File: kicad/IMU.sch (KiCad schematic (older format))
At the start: 3 parts, among them U6 ICM-20602

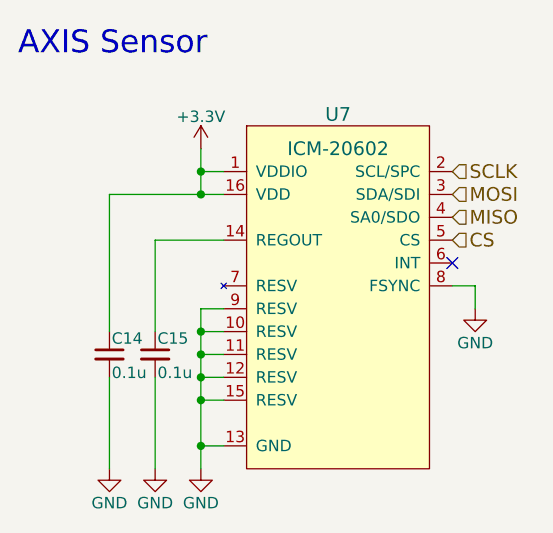
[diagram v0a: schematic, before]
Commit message: 回路にMA702を追加
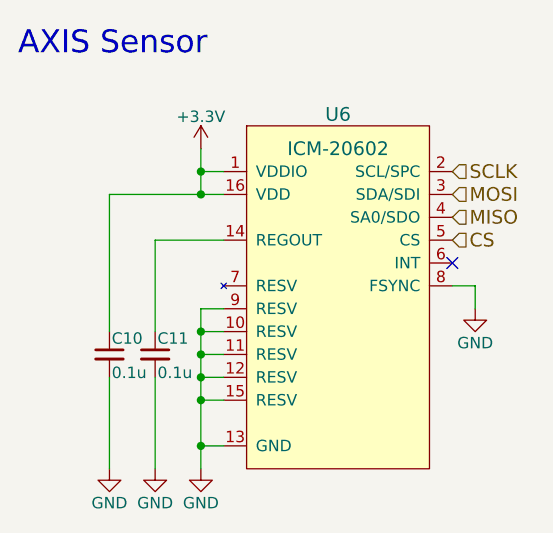
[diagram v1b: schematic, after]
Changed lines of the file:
@@
 AR Path="/57CC33F6/592C611A" Ref="U6"  Part="1"
 AR Path="/5A18D4D6/592C611A" Ref="U7"  Part="1"
-F 0 "U7" H 5600 4150 60  0000 C CNN
+F 0 "U6" H 5600 4150 60  0000 C CNN
 F 1 "ICM-20602" H 5600 4000 60  0000 C CNN
 F 2 "mouse:ICM-20602" H 5600 4000 60  0001 C CNN
@@
 AR Path="/57CC33F6/592C613A" Ref="C11"  Part="1"
 AR Path="/5A18D4D6/592C613A" Ref="C15"  Part="1"
-F 0 "C15" H 4810 3770 50  0000 L CNN
+F 0 "C11" H 4810 3770 50  0000 L CNN
 F 1 "0.1u" H 4810 3620 50  0000 L CNN
 F 2 "Capacitors_SMD:C_0201_NoSilk" H 4800 3700 50  0001 C CNN
@@
 AR Path="/57CC33F6/592C6186" Ref="C10"  Part="1"
 AR Path="/5A18D4D6/592C6186" Ref="C14"  Part="1"
-F 0 "C14" H 4610 3770 50  0000 L CNN
+F 0 "C10" H 4610 3770 50  0000 L CNN
 F 1 "0.1u" H 4610 3620 50  0000 L CNN
 F 2 "Capacitors_SMD:C_0201_NoSilk" H 4600 3700 50  0001 C CNN
@@
 AR Path="/57CC33F6/592C63E1" Ref="#PWR050"  Part="1"
 AR Path="/5A18D4D6/592C63E1" Ref="#PWR061"  Part="1"
-F 0 "#PWR061" H 5000 3950 50  0001 C CNN
+F 0 "#PWR050" H 5000 3950 50  0001 C CNN
 F 1 "GND" H 5000 4050 50  0000 C CNN
 F 2 "" H 5000 4200 50  0000 C CNN
@@
 AR Path="/57CC33F6/592C640D" Ref="#PWR048"  Part="1"
 AR Path="/5A18D4D6/592C640D" Ref="#PWR059"  Part="1"
-F 0 "#PWR059" H 4800 3950 50  0001 C CNN
+F 0 "#PWR048" H 4800 3950 50  0001 C CNN
 F 1 "GND" H 4800 4050 50  0000 C CNN
 F 2 "" H 4800 4200 50  0000 C CNN
@@
 AR Path="/57CC33F6/592C6444" Ref="#PWR047"  Part="1"
 AR Path="/5A18D4D6/592C6444" Ref="#PWR058"  Part="1"
-F 0 "#PWR058" H 4600 3950 50  0001 C CNN
+F 0 "#PWR047" H 4600 3950 50  0001 C CNN
 F 1 "GND" H 4600 4050 50  0000 C CNN
 F 2 "" H 4600 4200 50  0000 C CNN
@@
 AR Path="/57CC33F6/592C64FB" Ref="#PWR049"  Part="1"
 AR Path="/5A18D4D6/592C64FB" Ref="#PWR060"  Part="1"
-F 0 "#PWR060" H 5000 2650 50  0001 C CNN
+F 0 "#PWR049" H 5000 2650 50  0001 C CNN
 F 1 "+3.3V" H 5000 2940 50  0000 C CNN
 F 2 "" H 5000 2800 50  0000 C CNN
@@
 AR Path="/57CC33F6/592C6B85" Ref="#PWR051"  Part="1"
 AR Path="/5A18D4D6/592C6B85" Ref="#PWR062"  Part="1"
-F 0 "#PWR062" H 6200 3250 50  0001 C CNN
+F 0 "#PWR051" H 6200 3250 50  0001 C CNN
 F 1 "GND" H 6200 3350 50  0000 C CNN
 F 2 "" H 6200 3500 50  0000 C CNN

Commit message: コンデンサを追加
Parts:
- renumbered C10 to C11, C11 to C12
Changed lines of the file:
@@
 AR Path="/57CC33F6/592C611A" Ref="U6"  Part="1"
 AR Path="/5A18D4D6/592C611A" Ref="U7"  Part="1"
-F 0 "U6" H 5600 4150 60  0000 C CNN
+F 0 "U7" H 5600 4150 60  0000 C CNN
 F 1 "ICM-20602" H 5600 4000 60  0000 C CNN
 F 2 "mouse:ICM-20602" H 5600 4000 60  0001 C CNN
@@
 $EndComp
 $Comp
-L Device:C_Small C11
+L Device:C_Small C12
 U 1 1 592C613A
 P 4800 3700
-AR Path="/57CC33F6/592C613A" Ref="C11"  Part="1"
-AR Path="/5A18D4D6/592C613A" Ref="C15"  Part="1"
-F 0 "C11" H 4810 3770 50  0000 L CNN
+AR Path="/57CC33F6/592C613A" Ref="C12"  Part="1"
+AR Path="/5A18D4D6/592C613A" Ref="C16"  Part="1"
+F 0 "C16" H 4810 3770 50  0000 L CNN
 F 1 "0.1u" H 4810 3620 50  0000 L CNN
 F 2 "Capacitors_SMD:C_0201_NoSilk" H 4800 3700 50  0001 C CNN
@@
 $EndComp
 $Comp
-L Device:C_Small C10
+L Device:C_Small C11
 U 1 1 592C6186
 P 4600 3700
-AR Path="/57CC33F6/592C6186" Ref="C10"  Part="1"
-AR Path="/5A18D4D6/592C6186" Ref="C14"  Part="1"
-F 0 "C10" H 4610 3770 50  0000 L CNN
+AR Path="/57CC33F6/592C6186" Ref="C11"  Part="1"
+AR Path="/5A18D4D6/592C6186" Ref="C15"  Part="1"
+F 0 "C15" H 4610 3770 50  0000 L CNN
 F 1 "0.1u" H 4610 3620 50  0000 L CNN
 F 2 "Capacitors_SMD:C_0201_NoSilk" H 4600 3700 50  0001 C CNN
@@
 $EndComp
 $Comp
-L power:GND #PWR050
+L power:GND #PWR052
 U 1 1 592C63E1
 P 5000 4200
-AR Path="/57CC33F6/592C63E1" Ref="#PWR050"  Part="1"
-AR Path="/5A18D4D6/592C63E1" Ref="#PWR061"  Part="1"
-F 0 "#PWR061" H 5000 3950 50  0001 C CNN
+AR Path="/57CC33F6/592C63E1" Ref="#PWR052"  Part="1"
+AR Path="/5A18D4D6/592C63E1" Ref="#PWR063"  Part="1"
+F 0 "#PWR063" H 5000 3950 50  0001 C CNN
 F 1 "GND" H 5000 4050 50  0000 C CNN
 F 2 "" H 5000 4200 50  0000 C CNN
@@
 $EndComp
 $Comp
-L power:GND #PWR048
+L power:GND #PWR050
 U 1 1 592C640D
 P 4800 4200
-AR Path="/57CC33F6/592C640D" Ref="#PWR048"  Part="1"
-AR Path="/5A18D4D6/592C640D" Ref="#PWR059"  Part="1"
-F 0 "#PWR059" H 4800 3950 50  0001 C CNN
+AR Path="/57CC33F6/592C640D" Ref="#PWR050"  Part="1"
+AR Path="/5A18D4D6/592C640D" Ref="#PWR061"  Part="1"
+F 0 "#PWR061" H 4800 3950 50  0001 C CNN
 F 1 "GND" H 4800 4050 50  0000 C CNN
 F 2 "" H 4800 4200 50  0000 C CNN
@@
 $EndComp
 $Comp
-L power:GND #PWR047
+L power:GND #PWR049
 U 1 1 592C6444
 P 4600 4200
-AR Path="/57CC33F6/592C6444" Ref="#PWR047"  Part="1"
-AR Path="/5A18D4D6/592C6444" Ref="#PWR058"  Part="1"
-F 0 "#PWR058" H 4600 3950 50  0001 C CNN
+AR Path="/57CC33F6/592C6444" Ref="#PWR049"  Part="1"
+AR Path="/5A18D4D6/592C6444" Ref="#PWR060"  Part="1"
+F 0 "#PWR060" H 4600 3950 50  0001 C CNN
 F 1 "GND" H 4600 4050 50  0000 C CNN
 F 2 "" H 4600 4200 50  0000 C CNN
@@
 $EndComp
 $Comp
-L power:+3.3V #PWR049
+L power:+3.3V #PWR051
 U 1 1 592C64FB
 P 5000 2800
-AR Path="/57CC33F6/592C64FB" Ref="#PWR049"  Part="1"
-AR Path="/5A18D4D6/592C64FB" Ref="#PWR060"  Part="1"
-F 0 "#PWR060" H 5000 2650 50  0001 C CNN
+AR Path="/57CC33F6/592C64FB" Ref="#PWR051"  Part="1"
+AR Path="/5A18D4D6/592C64FB" Ref="#PWR062"  Part="1"
+F 0 "#PWR062" H 5000 2650 50  0001 C CNN
 F 1 "+3.3V" H 5000 2940 50  0000 C CNN
 F 2 "" H 5000 2800 50  0000 C CNN
@@
 NoConn ~ 6100 3300
 $Comp
-L power:GND #PWR051
+L power:GND #PWR053
 U 1 1 592C6B85
 P 6200 3500
-AR Path="/57CC33F6/592C6B85" Ref="#PWR051"  Part="1"
-AR Path="/5A18D4D6/592C6B85" Ref="#PWR062"  Part="1"
-F 0 "#PWR062" H 6200 3250 50  0001 C CNN
+AR Path="/57CC33F6/592C6B85" Ref="#PWR053"  Part="1"
+AR Path="/5A18D4D6/592C6B85" Ref="#PWR064"  Part="1"
+F 0 "#PWR064" H 6200 3250 50  0001 C CNN
 F 1 "GND" H 6200 3350 50  0000 C CNN
 F 2 "" H 6200 3500 50  0000 C CNN

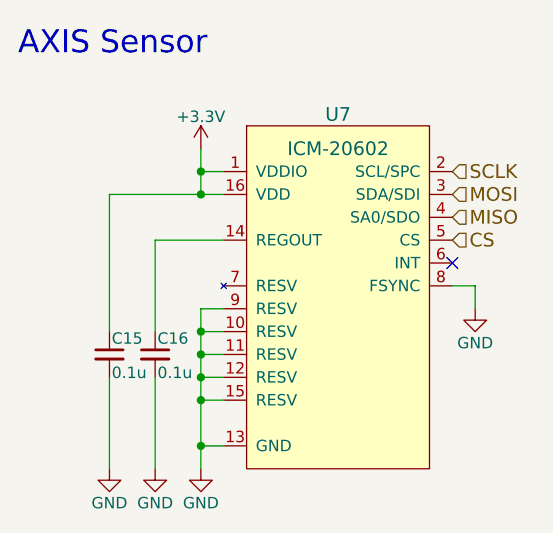
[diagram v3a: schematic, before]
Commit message: KERISEv4-5に向けて回路図を更新
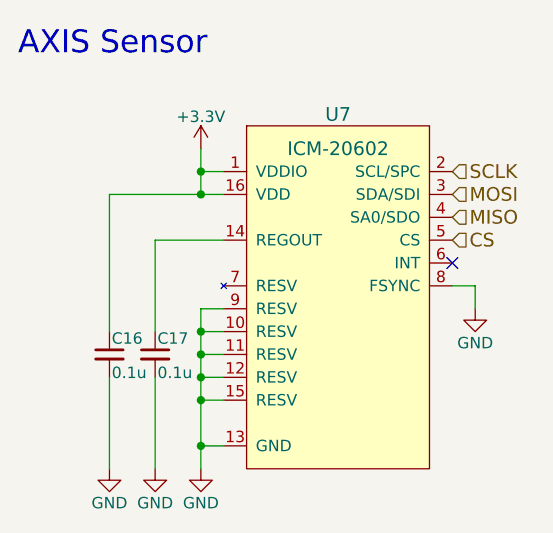
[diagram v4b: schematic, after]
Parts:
- renumbered C11 to C12, C12 to C13
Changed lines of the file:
@@
 $Descr A4 11693 8268
 encoding utf-8
-Sheet 10 14
+Sheet 10 15
 Title ""
 Date ""
@@
 $EndComp
 $Comp
-L Device:C_Small C12
+L Device:C_Small C13
 U 1 1 592C613A
 P 4800 3700
-AR Path="/57CC33F6/592C613A" Ref="C12"  Part="1"
-AR Path="/5A18D4D6/592C613A" Ref="C16"  Part="1"
-F 0 "C16" H 4810 3770 50  0000 L CNN
+AR Path="/57CC33F6/592C613A" Ref="C13"  Part="1"
+AR Path="/5A18D4D6/592C613A" Ref="C17"  Part="1"
+F 0 "C17" H 4810 3770 50  0000 L CNN
 F 1 "0.1u" H 4810 3620 50  0000 L CNN
 F 2 "Capacitors_SMD:C_0201_NoSilk" H 4800 3700 50  0001 C CNN
@@
 $EndComp
 $Comp
-L Device:C_Small C11
+L Device:C_Small C12
 U 1 1 592C6186
 P 4600 3700
-AR Path="/57CC33F6/592C6186" Ref="C11"  Part="1"
-AR Path="/5A18D4D6/592C6186" Ref="C15"  Part="1"
-F 0 "C15" H 4610 3770 50  0000 L CNN
+AR Path="/57CC33F6/592C6186" Ref="C12"  Part="1"
+AR Path="/5A18D4D6/592C6186" Ref="C16"  Part="1"
+F 0 "C16" H 4610 3770 50  0000 L CNN
 F 1 "0.1u" H 4610 3620 50  0000 L CNN
 F 2 "Capacitors_SMD:C_0201_NoSilk" H 4600 3700 50  0001 C CNN
@@
 $EndComp
 $Comp
-L power:GND #PWR052
+L power:GND #PWR054
 U 1 1 592C63E1
 P 5000 4200
-AR Path="/57CC33F6/592C63E1" Ref="#PWR052"  Part="1"
-AR Path="/5A18D4D6/592C63E1" Ref="#PWR063"  Part="1"
-F 0 "#PWR063" H 5000 3950 50  0001 C CNN
+AR Path="/57CC33F6/592C63E1" Ref="#PWR054"  Part="1"
+AR Path="/5A18D4D6/592C63E1" Ref="#PWR065"  Part="1"
+F 0 "#PWR065" H 5000 3950 50  0001 C CNN
 F 1 "GND" H 5000 4050 50  0000 C CNN
 F 2 "" H 5000 4200 50  0000 C CNN
@@
 $EndComp
 $Comp
-L power:GND #PWR050
+L power:GND #PWR052
 U 1 1 592C640D
 P 4800 4200
-AR Path="/57CC33F6/592C640D" Ref="#PWR050"  Part="1"
-AR Path="/5A18D4D6/592C640D" Ref="#PWR061"  Part="1"
-F 0 "#PWR061" H 4800 3950 50  0001 C CNN
+AR Path="/57CC33F6/592C640D" Ref="#PWR052"  Part="1"
+AR Path="/5A18D4D6/592C640D" Ref="#PWR063"  Part="1"
+F 0 "#PWR063" H 4800 3950 50  0001 C CNN
 F 1 "GND" H 4800 4050 50  0000 C CNN
 F 2 "" H 4800 4200 50  0000 C CNN
@@
 $EndComp
 $Comp
-L power:GND #PWR049
+L power:GND #PWR051
 U 1 1 592C6444
 P 4600 4200
-AR Path="/57CC33F6/592C6444" Ref="#PWR049"  Part="1"
-AR Path="/5A18D4D6/592C6444" Ref="#PWR060"  Part="1"
-F 0 "#PWR060" H 4600 3950 50  0001 C CNN
+AR Path="/57CC33F6/592C6444" Ref="#PWR051"  Part="1"
+AR Path="/5A18D4D6/592C6444" Ref="#PWR062"  Part="1"
+F 0 "#PWR062" H 4600 3950 50  0001 C CNN
 F 1 "GND" H 4600 4050 50  0000 C CNN
 F 2 "" H 4600 4200 50  0000 C CNN
@@
 $EndComp
 $Comp
-L power:+3.3V #PWR051
+L power:+3.3V #PWR053
 U 1 1 592C64FB
 P 5000 2800
-AR Path="/57CC33F6/592C64FB" Ref="#PWR051"  Part="1"
-AR Path="/5A18D4D6/592C64FB" Ref="#PWR062"  Part="1"
-F 0 "#PWR062" H 5000 2650 50  0001 C CNN
+AR Path="/57CC33F6/592C64FB" Ref="#PWR053"  Part="1"
+AR Path="/5A18D4D6/592C64FB" Ref="#PWR064"  Part="1"
+F 0 "#PWR064" H 5000 2650 50  0001 C CNN
 F 1 "+3.3V" H 5000 2940 50  0000 C CNN
 F 2 "" H 5000 2800 50  0000 C CNN
@@
 NoConn ~ 6100 3300
 $Comp
-L power:GND #PWR053
+L power:GND #PWR055
 U 1 1 592C6B85
 P 6200 3500
-AR Path="/57CC33F6/592C6B85" Ref="#PWR053"  Part="1"
-AR Path="/5A18D4D6/592C6B85" Ref="#PWR064"  Part="1"
-F 0 "#PWR064" H 6200 3250 50  0001 C CNN
+AR Path="/57CC33F6/592C6B85" Ref="#PWR055"  Part="1"
+AR Path="/5A18D4D6/592C6B85" Ref="#PWR066"  Part="1"
+F 0 "#PWR066" H 6200 3250 50  0001 C CNN
 F 1 "GND" H 6200 3350 50  0000 C CNN
 F 2 "" H 6200 3500 50  0000 C CNN

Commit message: フットプリントを割り当て
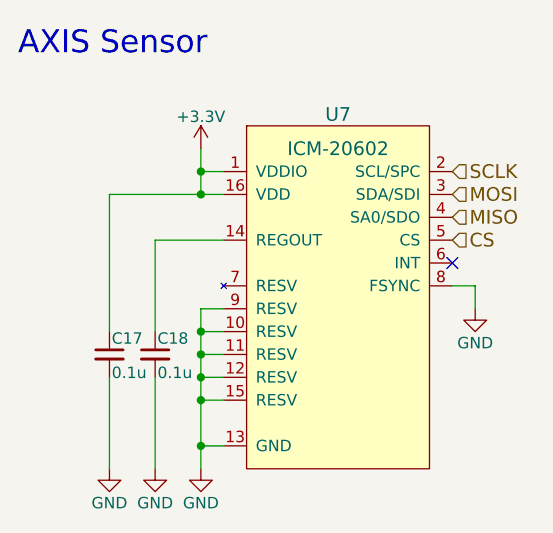
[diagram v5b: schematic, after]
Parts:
- C13: renamed from C12; footprint Capacitors_SMD:C_0201_NoSilk -> Capacitor_SMD:C_0201_0603Metric
- C14: renamed from C13; footprint Capacitors_SMD:C_0201_NoSilk -> Capacitor_SMD:C_0201_0603Metric
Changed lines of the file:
@@
 $EndComp
 $Comp
-L Device:C_Small C13
+L Device:C_Small C14
 U 1 1 592C613A
 P 4800 3700
-AR Path="/57CC33F6/592C613A" Ref="C13"  Part="1"
-AR Path="/5A18D4D6/592C613A" Ref="C17"  Part="1"
-F 0 "C17" H 4810 3770 50  0000 L CNN
+AR Path="/57CC33F6/592C613A" Ref="C14"  Part="1"
+AR Path="/5A18D4D6/592C613A" Ref="C18"  Part="1"
+F 0 "C18" H 4810 3770 50  0000 L CNN
 F 1 "0.1u" H 4810 3620 50  0000 L CNN
-F 2 "Capacitors_SMD:C_0201_NoSilk" H 4800 3700 50  0001 C CNN
+F 2 "Capacitor_SMD:C_0201_0603Metric" H 4800 3700 50  0001 C CNN
 F 3 "" H 4800 3700 50  0000 C CNN
 	1    4800 3700
@@
 $EndComp
 $Comp
-L Device:C_Small C12
+L Device:C_Small C13
 U 1 1 592C6186
 P 4600 3700
-AR Path="/57CC33F6/592C6186" Ref="C12"  Part="1"
-AR Path="/5A18D4D6/592C6186" Ref="C16"  Part="1"
-F 0 "C16" H 4610 3770 50  0000 L CNN
+AR Path="/57CC33F6/592C6186" Ref="C13"  Part="1"
+AR Path="/5A18D4D6/592C6186" Ref="C17"  Part="1"
+F 0 "C17" H 4610 3770 50  0000 L CNN
 F 1 "0.1u" H 4610 3620 50  0000 L CNN
-F 2 "Capacitors_SMD:C_0201_NoSilk" H 4600 3700 50  0001 C CNN
+F 2 "Capacitor_SMD:C_0201_0603Metric" H 4600 3700 50  0001 C CNN
 F 3 "" H 4600 3700 50  0000 C CNN
 	1    4600 3700
@@
 $EndComp
 $Comp
-L power:GND #PWR054
+L power:GND #PWR056
 U 1 1 592C63E1
 P 5000 4200
-AR Path="/57CC33F6/592C63E1" Ref="#PWR054"  Part="1"
-AR Path="/5A18D4D6/592C63E1" Ref="#PWR065"  Part="1"
-F 0 "#PWR065" H 5000 3950 50  0001 C CNN
+AR Path="/57CC33F6/592C63E1" Ref="#PWR056"  Part="1"
+AR Path="/5A18D4D6/592C63E1" Ref="#PWR067"  Part="1"
+F 0 "#PWR067" H 5000 3950 50  0001 C CNN
 F 1 "GND" H 5000 4050 50  0000 C CNN
 F 2 "" H 5000 4200 50  0000 C CNN
@@
 $EndComp
 $Comp
-L power:GND #PWR052
+L power:GND #PWR054
 U 1 1 592C640D
 P 4800 4200
-AR Path="/57CC33F6/592C640D" Ref="#PWR052"  Part="1"
-AR Path="/5A18D4D6/592C640D" Ref="#PWR063"  Part="1"
-F 0 "#PWR063" H 4800 3950 50  0001 C CNN
+AR Path="/57CC33F6/592C640D" Ref="#PWR054"  Part="1"
+AR Path="/5A18D4D6/592C640D" Ref="#PWR065"  Part="1"
+F 0 "#PWR065" H 4800 3950 50  0001 C CNN
 F 1 "GND" H 4800 4050 50  0000 C CNN
 F 2 "" H 4800 4200 50  0000 C CNN
@@
 $EndComp
 $Comp
-L power:GND #PWR051
+L power:GND #PWR053
 U 1 1 592C6444
 P 4600 4200
-AR Path="/57CC33F6/592C6444" Ref="#PWR051"  Part="1"
-AR Path="/5A18D4D6/592C6444" Ref="#PWR062"  Part="1"
-F 0 "#PWR062" H 4600 3950 50  0001 C CNN
+AR Path="/57CC33F6/592C6444" Ref="#PWR053"  Part="1"
+AR Path="/5A18D4D6/592C6444" Ref="#PWR064"  Part="1"
+F 0 "#PWR064" H 4600 3950 50  0001 C CNN
 F 1 "GND" H 4600 4050 50  0000 C CNN
 F 2 "" H 4600 4200 50  0000 C CNN
@@
 $EndComp
 $Comp
-L power:+3.3V #PWR053
+L power:+3.3V #PWR055
 U 1 1 592C64FB
 P 5000 2800
-AR Path="/57CC33F6/592C64FB" Ref="#PWR053"  Part="1"
-AR Path="/5A18D4D6/592C64FB" Ref="#PWR064"  Part="1"
-F 0 "#PWR064" H 5000 2650 50  0001 C CNN
+AR Path="/57CC33F6/592C64FB" Ref="#PWR055"  Part="1"
+AR Path="/5A18D4D6/592C64FB" Ref="#PWR066"  Part="1"
+F 0 "#PWR066" H 5000 2650 50  0001 C CNN
 F 1 "+3.3V" H 5000 2940 50  0000 C CNN
 F 2 "" H 5000 2800 50  0000 C CNN
@@
 NoConn ~ 6100 3300
 $Comp
-L power:GND #PWR055
+L power:GND #PWR057
 U 1 1 592C6B85
 P 6200 3500
-AR Path="/57CC33F6/592C6B85" Ref="#PWR055"  Part="1"
-AR Path="/5A18D4D6/592C6B85" Ref="#PWR066"  Part="1"
-F 0 "#PWR066" H 6200 3250 50  0001 C CNN
+AR Path="/57CC33F6/592C6B85" Ref="#PWR057"  Part="1"
+AR Path="/5A18D4D6/592C6B85" Ref="#PWR068"  Part="1"
+F 0 "#PWR068" H 6200 3250 50  0001 C CNN
 F 1 "GND" H 6200 3350 50  0000 C CNN
 F 2 "" H 6200 3500 50  0000 C CNN

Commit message: 部品を配置
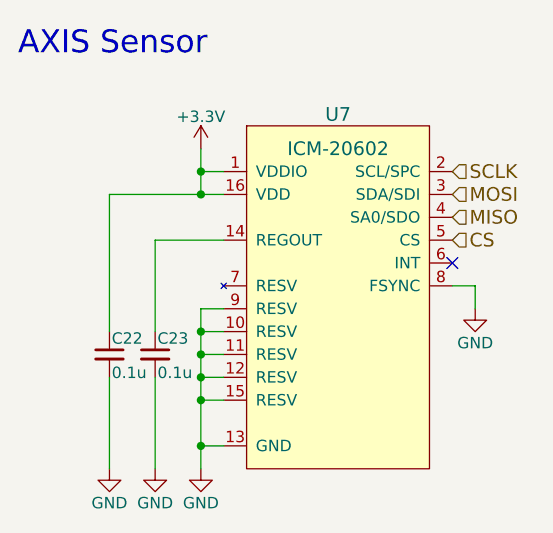
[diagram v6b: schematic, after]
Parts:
- renumbered C13 to C16, C14 to C17
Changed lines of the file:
@@
 $EndComp
 $Comp
-L Device:C_Small C14
+L Device:C_Small C17
 U 1 1 592C613A
 P 4800 3700
-AR Path="/57CC33F6/592C613A" Ref="C14"  Part="1"
-AR Path="/5A18D4D6/592C613A" Ref="C18"  Part="1"
-F 0 "C18" H 4810 3770 50  0000 L CNN
+AR Path="/57CC33F6/592C613A" Ref="C17"  Part="1"
+AR Path="/5A18D4D6/592C613A" Ref="C23"  Part="1"
+F 0 "C23" H 4810 3770 50  0000 L CNN
 F 1 "0.1u" H 4810 3620 50  0000 L CNN
 F 2 "Capacitor_SMD:C_0201_0603Metric" H 4800 3700 50  0001 C CNN
@@
 $EndComp
 $Comp
-L Device:C_Small C13
+L Device:C_Small C16
 U 1 1 592C6186
 P 4600 3700
-AR Path="/57CC33F6/592C6186" Ref="C13"  Part="1"
-AR Path="/5A18D4D6/592C6186" Ref="C17"  Part="1"
-F 0 "C17" H 4610 3770 50  0000 L CNN
+AR Path="/57CC33F6/592C6186" Ref="C16"  Part="1"
+AR Path="/5A18D4D6/592C6186" Ref="C22"  Part="1"
+F 0 "C22" H 4610 3770 50  0000 L CNN
 F 1 "0.1u" H 4610 3620 50  0000 L CNN
 F 2 "Capacitor_SMD:C_0201_0603Metric" H 4600 3700 50  0001 C CNN
@@
 $EndComp
 $Comp
-L power:GND #PWR056
+L power:GND #PWR058
 U 1 1 592C63E1
 P 5000 4200
-AR Path="/57CC33F6/592C63E1" Ref="#PWR056"  Part="1"
-AR Path="/5A18D4D6/592C63E1" Ref="#PWR067"  Part="1"
-F 0 "#PWR067" H 5000 3950 50  0001 C CNN
+AR Path="/57CC33F6/592C63E1" Ref="#PWR058"  Part="1"
+AR Path="/5A18D4D6/592C63E1" Ref="#PWR069"  Part="1"
+F 0 "#PWR069" H 5000 3950 50  0001 C CNN
 F 1 "GND" H 5000 4050 50  0000 C CNN
 F 2 "" H 5000 4200 50  0000 C CNN
@@
 $EndComp
 $Comp
-L power:GND #PWR054
+L power:GND #PWR056
 U 1 1 592C640D
 P 4800 4200
-AR Path="/57CC33F6/592C640D" Ref="#PWR054"  Part="1"
-AR Path="/5A18D4D6/592C640D" Ref="#PWR065"  Part="1"
-F 0 "#PWR065" H 4800 3950 50  0001 C CNN
+AR Path="/57CC33F6/592C640D" Ref="#PWR056"  Part="1"
+AR Path="/5A18D4D6/592C640D" Ref="#PWR067"  Part="1"
+F 0 "#PWR067" H 4800 3950 50  0001 C CNN
 F 1 "GND" H 4800 4050 50  0000 C CNN
 F 2 "" H 4800 4200 50  0000 C CNN
@@
 $EndComp
 $Comp
-L power:GND #PWR053
+L power:GND #PWR055
 U 1 1 592C6444
 P 4600 4200
-AR Path="/57CC33F6/592C6444" Ref="#PWR053"  Part="1"
-AR Path="/5A18D4D6/592C6444" Ref="#PWR064"  Part="1"
-F 0 "#PWR064" H 4600 3950 50  0001 C CNN
+AR Path="/57CC33F6/592C6444" Ref="#PWR055"  Part="1"
+AR Path="/5A18D4D6/592C6444" Ref="#PWR066"  Part="1"
+F 0 "#PWR066" H 4600 3950 50  0001 C CNN
 F 1 "GND" H 4600 4050 50  0000 C CNN
 F 2 "" H 4600 4200 50  0000 C CNN
@@
 $EndComp
 $Comp
-L power:+3.3V #PWR055
+L power:+3.3V #PWR057
 U 1 1 592C64FB
 P 5000 2800
-AR Path="/57CC33F6/592C64FB" Ref="#PWR055"  Part="1"
-AR Path="/5A18D4D6/592C64FB" Ref="#PWR066"  Part="1"
-F 0 "#PWR066" H 5000 2650 50  0001 C CNN
+AR Path="/57CC33F6/592C64FB" Ref="#PWR057"  Part="1"
+AR Path="/5A18D4D6/592C64FB" Ref="#PWR068"  Part="1"
+F 0 "#PWR068" H 5000 2650 50  0001 C CNN
 F 1 "+3.3V" H 5000 2940 50  0000 C CNN
 F 2 "" H 5000 2800 50  0000 C CNN
@@
 NoConn ~ 6100 3300
 $Comp
-L power:GND #PWR057
+L power:GND #PWR059
 U 1 1 592C6B85
 P 6200 3500
-AR Path="/57CC33F6/592C6B85" Ref="#PWR057"  Part="1"
-AR Path="/5A18D4D6/592C6B85" Ref="#PWR068"  Part="1"
-F 0 "#PWR068" H 6200 3250 50  0001 C CNN
+AR Path="/57CC33F6/592C6B85" Ref="#PWR059"  Part="1"
+AR Path="/5A18D4D6/592C6B85" Ref="#PWR070"  Part="1"
+F 0 "#PWR070" H 6200 3250 50  0001 C CNN
 F 1 "GND" H 6200 3350 50  0000 C CNN
 F 2 "" H 6200 3500 50  0000 C CNN
